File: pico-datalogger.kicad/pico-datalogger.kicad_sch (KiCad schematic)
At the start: 15 parts, among them J1 JST-PH2 VCC, J4 Alt-VCC, SW1 SW_Push_SLIM, U1 SN74HC74N, Y1 Crystal

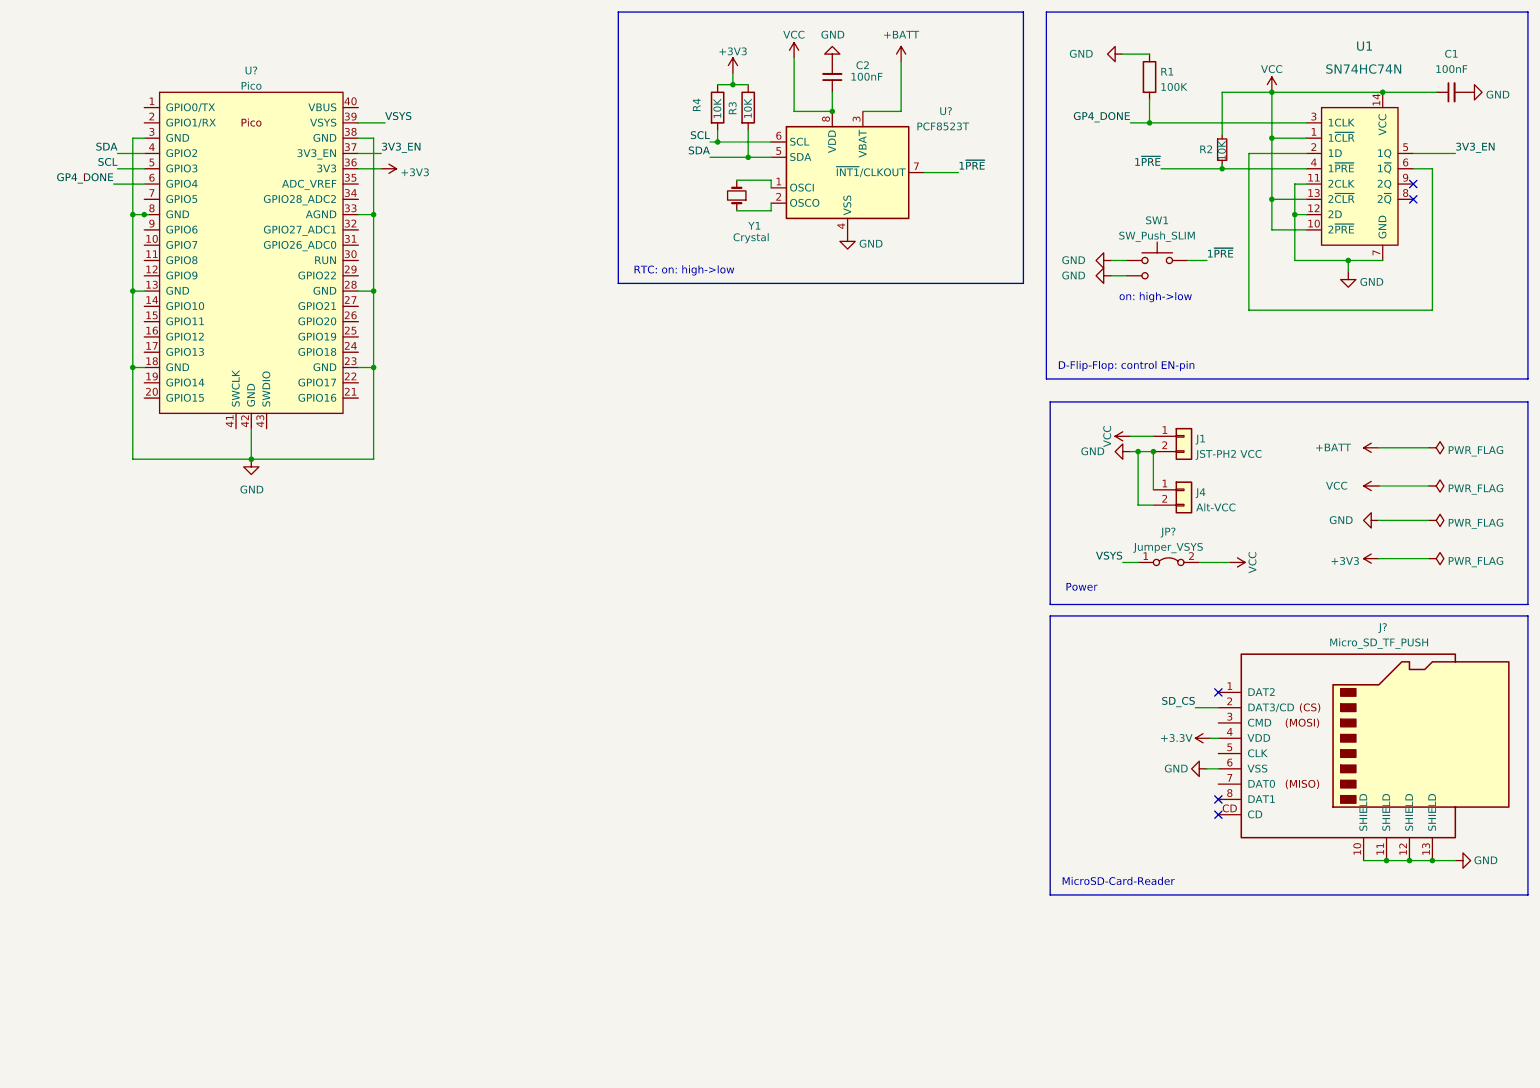
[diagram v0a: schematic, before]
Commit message: added battery and connectors
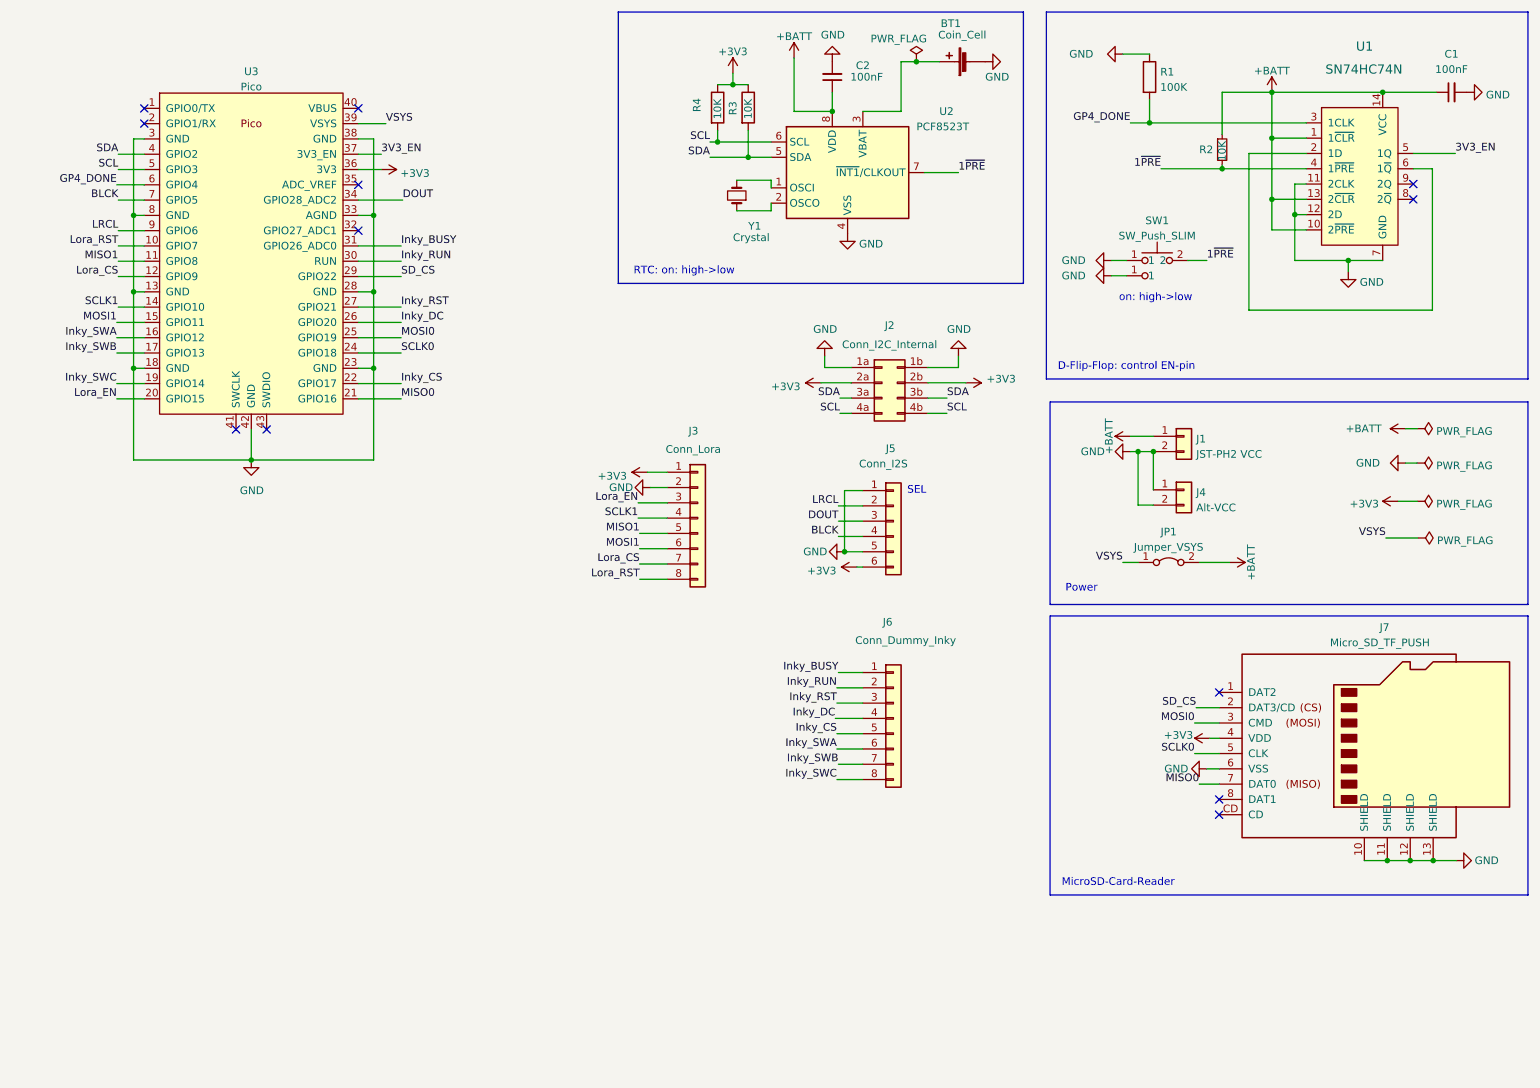
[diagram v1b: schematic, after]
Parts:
- added BT1: Coin_Cell, symbol Device:Battery_Cell
- added J2: Conn_I2C_Internal, symbol Connector_Generic:Conn_02x04_Row_Letter_Last
- added J3: Conn_Lora, symbol Connector_Generic:Conn_01x08
- added J5: Conn_I2S, symbol Connector_Generic:Conn_01x06
- added J6: Conn_Dummy_Inky, symbol Connector_Generic:Conn_01x08
- gave numbers to parts that had none: 4
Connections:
- net +3.3V is gone; now on net +3V3: J7.4 (VDD)
- net VCC is gone; now on net +BATT: C1.1, C2.1, J1.1 (Pin_1), JP1.2 (B), R2.1, U1.1 (1~{CLR}), U1.10 (2~{PRE}), U1.13 (2~{CLR}), U1.14 (VCC), U2.8 (VDD)
- net +3V3: now also J2.2a (Pin_2a), J2.2b (Pin_2b), J3.1 (Pin_1), J5.6 (Pin_6)
- net +BATT: no longer U2.3 (VBAT)
- net GND: now also BT1.2 (-), J2.1a (Pin_1a), J2.1b (Pin_1b), J3.2 (Pin_2), J5.1 (Pin_1), J5.5 (Pin_5); no longer SW1.3 (1)
- net SCL: now also J2.4a (Pin_4a), J2.4b (Pin_4b)
- net SDA: now also J2.3a (Pin_3a), J2.3b (Pin_3b)
- net SD_CS: now also U3.29 (GPIO22)
- net MOSI0: now reaches J7.3 (CMD)
- net MOSI0: now also U3.25 (GPIO19)
- net SCLK0: now reaches J7.5 (CLK)
- net SCLK0: now also U3.24 (GPIO18)
- net MISO0: now reaches J7.7 (DAT0)
- net MISO0: now also U3.21 (GPIO16)
- net Lora_RST: now reaches U3.10 (GPIO7)
- net Lora_RST: now also J3.8 (Pin_8)
- net MISO1: now reaches U3.11 (GPIO8)
- net MISO1: now also J3.5 (Pin_5)
- net Lora_CS: now reaches U3.12 (GPIO9)
- net Lora_CS: now also J3.7 (Pin_7)
- net SCLK1: now reaches U3.14 (GPIO10)
- net SCLK1: now also J3.4 (Pin_4)
- net MOSI1: now reaches U3.15 (GPIO11)
- net MOSI1: now also J3.6 (Pin_6)
- net Inky_SWA: now reaches U3.16 (GPIO12)
- net Inky_SWA: now also J6.6 (Pin_6)
- net Inky_SWB: now reaches U3.17 (GPIO13)
- net Inky_SWB: now also J6.7 (Pin_7)
- net Inky_SWC: now reaches U3.19 (GPIO14)
- net Inky_SWC: now also J6.8 (Pin_8)
- net Lora_EN: now reaches U3.20 (GPIO15)
- net Lora_EN: now also J3.3 (Pin_3)
- net Inky_CS: now reaches U3.22 (GPIO17)
- net Inky_CS: now also J6.5 (Pin_5)
- net Inky_DC: now reaches U3.26 (GPIO20)
- net Inky_DC: now also J6.4 (Pin_4)
- net Inky_RST: now reaches U3.27 (GPIO21)
- net Inky_RST: now also J6.3 (Pin_3)
- net Inky_RUN: now reaches U3.30 (RUN)
- net Inky_RUN: now also J6.2 (Pin_2)
- net Inky_BUSY: now reaches U3.31 (GPIO26_ADC0)
- net Inky_BUSY: now also J6.1 (Pin_1)
- net DOUT: now reaches U3.34 (GPIO28_ADC2)
- net DOUT: now also J5.3 (Pin_3)
- net BLCK: now reaches U3.7 (GPIO5)
- net BLCK: now also J5.4 (Pin_4)
- net LRCL: now reaches U3.9 (GPIO6)
- net LRCL: now also J5.2 (Pin_2)
- new net: BT1.1 (+), U2.3 (VBAT)
- no-connect marks 5 -> 12
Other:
- note added: "SEL"

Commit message: Rev. 0.8: components with footprints
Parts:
- BT1: footprint (none) -> user:CR2032_Holder; LCSC (none) -> C964777
- J2: footprint (none) -> Connector_PinHeader_2.54mm:PinHeader_2x04_P2.54mm_Vertical; now left out of the parts list
- J3: value Conn_Lora -> RFM9x_Lora_Breakout; footprint (none) -> user:RFM9x_Lora_Breakout; symbol Connector_Generic:Conn_01x08 -> user:RFM9x_Lora_Breakout
- J5: footprint (none) -> Connector_PinHeader_2.54mm:PinHeader_1x06_P2.54mm_Vertical; now left out of the parts list
- J6, U3: now left out of the parts list
- JP1: footprint (none) -> user:CR2032_Holder
- U2: LCSC C7440 -> C2651516
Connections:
- net Lora_CS: now also J3.8 (CS); no longer J3.7 (Pin_7)
- net Lora_RST: now also J3.9 (RST); no longer J3.8 (Pin_8)
- net MISO1: now also J3.6 (MISO); no longer J3.5 (Pin_5)
- net MOSI1: now also J3.7 (MOSI); no longer J3.6 (Pin_6)
- net SCLK1: now also J3.5 (SCK); no longer J3.4 (Pin_4)
- no-connect marks 12 -> 18
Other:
- note added: "Connectors (addons)"
- note added: "Connectors (internal)"
- note added: "Pico (2x20 Header)"
- moved on the sheet: J5, J6, U3

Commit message: Rev. 0.9: initial routing
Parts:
- J2: symbol Connector_Generic:Conn_02x04_Row_Letter_Last -> Connector_Generic:Conn_02x04_Odd_Even; now in the parts list
- JP1: footprint user:CR2032_Holder -> Connector_PinHeader_2.54mm:PinHeader_1x02_P2.54mm_Vertical
- U3: footprint RPi_Pico:RPi_Pico_SMD_TH -> user:RPi_Pico_TH_nodbg
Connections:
- net +3V3: now also J2.3 (Pin_3), J2.4 (Pin_4); no longer J2.2a (Pin_2a), J2.2b (Pin_2b)
- net +BATT: now also J4.1 (Pin_1)
- net GND: now also J2.1 (Pin_1), J2.2 (Pin_2); no longer J2.1a (Pin_1a), J2.1b (Pin_1b), J4.1 (Pin_1)
- net SCL: now also J2.7 (Pin_7), J2.8 (Pin_8); no longer J2.4a (Pin_4a), J2.4b (Pin_4b)
- net SDA: now also J2.5 (Pin_5), J2.6 (Pin_6); no longer J2.3a (Pin_3a), J2.3b (Pin_3b)

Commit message: Rev. 0.95: review for production
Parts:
- added H1, H2, H3, H4: MountingHole, MountingHole:MountingHole_2.5mm, symbol Mechanical:MountingHole
- added J10: Conn_Inky_SW, Connector_PinHeader_2.54mm:PinHeader_1x03_P2.54mm_Vertical, symbol Connector_Generic:Conn_01x03
- added J8: Conn_ADC, Connector_PinHeader_2.54mm:PinHeader_1x03_P2.54mm_Horizontal, symbol Connector_Generic:Conn_01x03
- added J9: Conn_UART, Connector_PinHeader_2.54mm:PinHeader_1x04_P2.54mm_Horizontal, symbol Connector_Generic:Conn_01x04
- J6: value Conn_Dummy_Inky -> Conn_Inky_SPI; footprint (none) -> Connector_PinHeader_2.54mm:PinHeader_1x08_P2.54mm_Vertical
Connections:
- net +3V3: now also J8.1 (Pin_1), J9.3 (Pin_3)
- net GND: now also J8.2 (Pin_2), J9.4 (Pin_4)
- net Inky_CS: now also J6.7 (Pin_7); no longer J6.5 (Pin_5)
- net Inky_SWA: now also J10.1 (Pin_1); no longer J6.6 (Pin_6)
- net Inky_SWB: now also J10.2 (Pin_2); no longer J6.7 (Pin_7)
- net Inky_SWC: now also J10.3 (Pin_3); no longer J6.8 (Pin_8)
- net MISO0: now also J6.8 (Pin_8)
- net MOSI0: now also J6.5 (Pin_5)
- net SCLK0: now also J6.6 (Pin_6)
- net TX: now reaches U3.1 (GPIO0/TX)
- net TX: now also J9.2 (Pin_2)
- net RX: now reaches U3.2 (GPIO1/RX)
- net RX: now also J9.1 (Pin_1)
- net GP27_ADC1: now reaches U3.32 (GPIO27_ADC1)
- net GP27_ADC1: now also J8.3 (Pin_3)
- no-connect marks 18 -> 15
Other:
- note added: "Connector Inky (optional)"
- note added: "Pico (2x20 Stacking-Header)"
- note removed: "Pico (2x20 Header)"
- moved on the sheet: J1, J4, J6

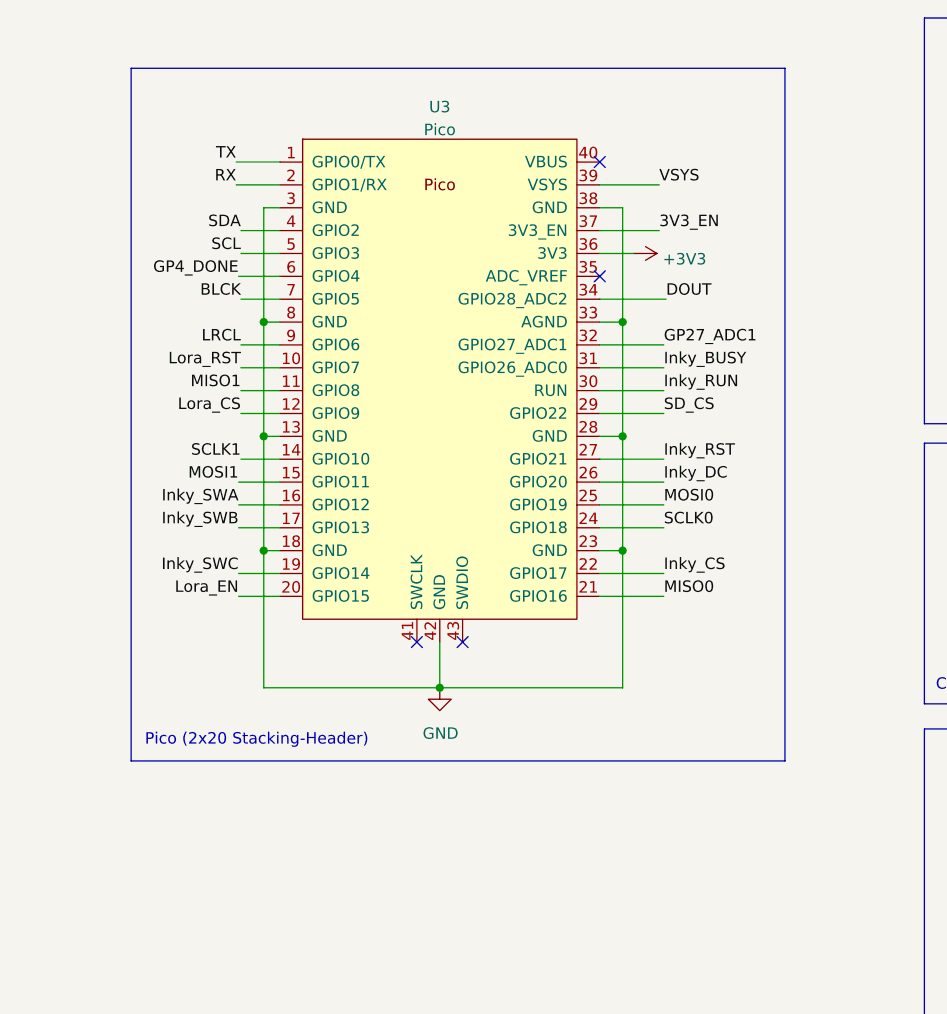
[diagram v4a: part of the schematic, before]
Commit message: Rev 0.96: added reset-button
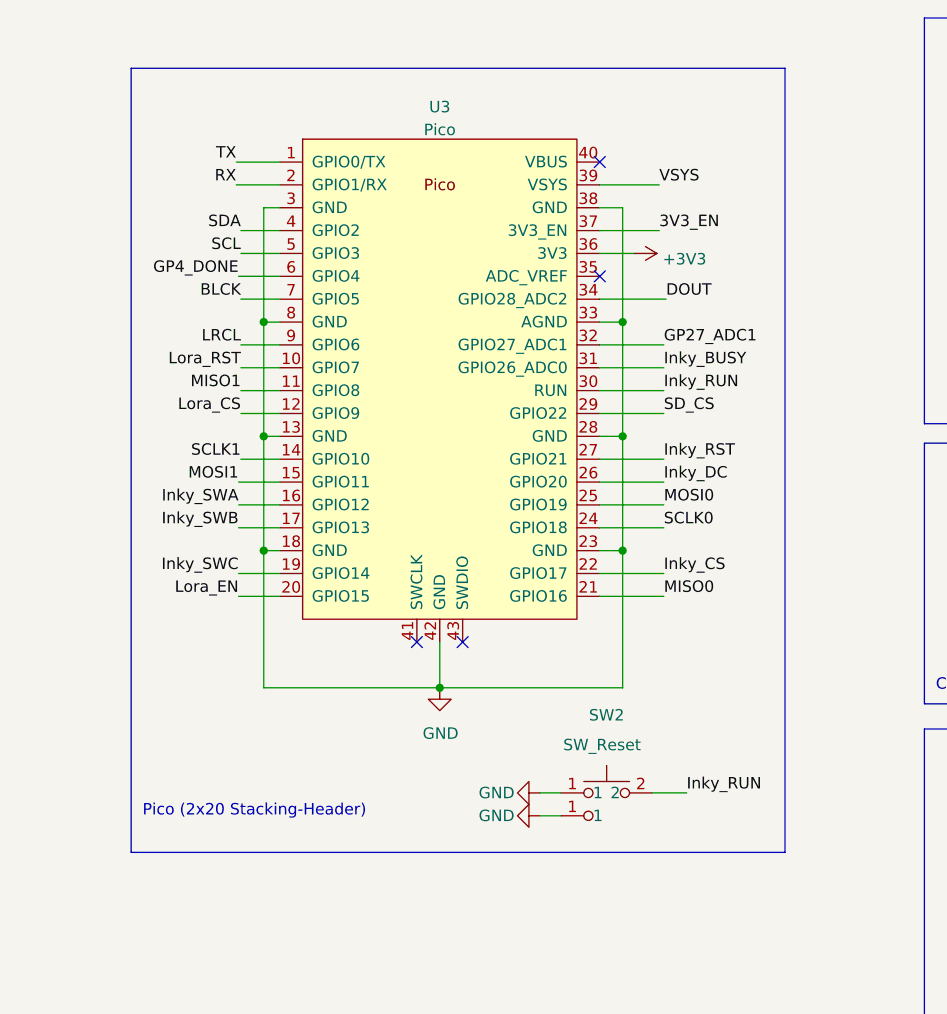
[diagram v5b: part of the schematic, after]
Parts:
- added SW2: SW_Reset, user:SW_PUSH_SLIM_1x4, symbol user:SW_Push_SLIM
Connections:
- net GND: now also SW2.1
- net Inky_RUN: now also SW2.2
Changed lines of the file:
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@@
   (title_block
     (title "pico-datalogger")
-    (date "2023-05-13")
-    (rev "0.95")
+    (date "2023-05-14")
+    (rev "0.96")
     (company "Bernhard Bablok")
     (comment 1 "https://github.com/bablokb/pcb-pico-datalogger")
@@
     (stroke (width 0) (type default) (color 0 0 0 0))
   )
+  (wire (pts (xy 85.598 106.426) (xy 87.884 106.426))
+    (stroke (width 0) (type default) (color 0 0 0 0))
+  )
   (wire (pts (xy 138.938 119.126) (xy 143.51 119.126))
     (stroke (width 0) (type default) (color 0 0 0 0))
@@
     (stroke (width 0) (type default) (color 0 0 0 0))
   )
-  (polyline (pts (xy 40.132 23.368) (xy 40.132 100.33))
+  (polyline (pts (xy 40.132 23.368) (xy 40.132 110.49))
     (stroke (width 0) (type default) (color 0 0 0 0))
   )
@@
     (stroke (width 0) (type default) (color 0 0 0 0))
   )
-  (polyline (pts (xy 112.776 23.368) (xy 112.776 100.33))
+  (polyline (pts (xy 112.776 23.368) (xy 112.776 110.49))
     (stroke (width 0) (type default) (color 0 0 0 0))
   )
@@
     (stroke (width 0) (type default) (color 0 0 0 0))
   )
+  (wire (pts (xy 101.854 103.886) (xy 98.044 103.886))
+    (stroke (width 0) (type default) (color 0 0 0 0))
+  )
   (wire (pts (xy 99.314 74.422) (xy 92.202 74.422))
     (stroke (width 0) (type default) (color 0 0 0 0))
@@
     (stroke (width 0) (type default) (color 0 0 0 0))
   )
-  (polyline (pts (xy 112.776 100.33) (xy 40.132 100.33))
+  (polyline (pts (xy 112.776 110.49) (xy 40.132 110.49))
     (stroke (width 0) (type default) (color 0 0 0 0))
   )
@@
     (stroke (width 0) (type default) (color 0 0 0 0))
   )
+  (wire (pts (xy 85.598 103.886) (xy 87.884 103.886))
+    (stroke (width 0) (type default) (color 0 0 0 0))
+  )
   (wire (pts (xy 153.67 50.8) (xy 147.955 50.8))
     (stroke (width 0) (type default) (color 0 0 0 0))
@@
     (effects (font (size 1.27 1.27)) (justify left bottom))
   )
-  (text "Pico (2x20 Stacking-Header)" (at 41.656 98.806 0)
+  (text "Pico (2x20 Stacking-Header)" (at 41.402 106.68 0)
     (effects (font (size 1.27 1.27)) (justify left bottom))
   )
@@
   (label "VSYS" (at 212.09 109.22 180)
     (effects (font (size 1.27 1.27)) (justify right bottom))
+  )
+  (label "Inky_RUN" (at 101.854 103.886 0)
+    (effects (font (size 1.27 1.27)) (justify left bottom))
   )
   (label "SCL" (at 52.324 43.942 180)
@@
     )
     (property "Datasheet" "" (id 3) (at 180.594 127.762 0)
+      (effects (font (size 1.27 1.27)) hide)
+    )
+    (pin "1")
+  )
+  (symbol (lib_id "power:GND") (at 85.598 103.886 270) (unit 1)
+    (in_bom yes) (on_board yes)
+    (property "Reference" "#PWR029" (id 0) (at 79.248 103.886 0)
+      (effects (font (size 1.27 1.27)) hide)
+    )
+    (property "Value" "GND" (id 1) (at 78.74 103.886 90)
+      (effects (font (size 1.27 1.27)) (justify left))
+    )
+    (property "Footprint" "" (id 2) (at 85.598 103.886 0)
+      (effects (font (size 1.27 1.27)) hide)
+    )
+    (property "Datasheet" "" (id 3) (at 85.598 103.886 0)
       (effects (font (size 1.27 1.27)) hide)
     )
@@
     )
     (pin "1")
+  )
+  (symbol (lib_id "user:SW_Push_SLIM") (at 92.964 103.886 0) (unit 1)
+    (in_bom yes) (on_board yes)
+    (property "Reference" "SW2" (id 0) (at 92.964 95.25 0))
+    (property "Value" "SW_Reset" (id 1) (at 92.456 98.552 0))
+    (property "Footprint" "user:SW_PUSH_SLIM_1x4" (id 2) (at 92.964 111.506 0)
+      (effects (font (size 1.27 1.27)) hide)
+    )
+    (property "Datasheet" "" (id 3) (at 92.964 98.806 0)
+      (effects (font (size 1.27 1.27)) hide)
+    )
+    (pin "1")
+    (pin "1")
+    (pin "2")
   )
   (symbol (lib_id "power:GND") (at 189.23 26.035 90) (unit 1)
@@
     )
     (property "Datasheet" "" (id 3) (at 142.24 83.82 0)
+      (effects (font (size 1.27 1.27)) hide)
+    )
+    (pin "1")
+  )
+  (symbol (lib_id "power:GND") (at 85.598 106.426 270) (unit 1)
+    (in_bom yes) (on_board yes)
+    (property "Reference" "#PWR030" (id 0) (at 79.248 106.426 0)
+      (effects (font (size 1.27 1.27)) hide)
+    )
+    (property "Value" "GND" (id 1) (at 78.74 106.426 90)
+      (effects (font (size 1.27 1.27)) (justify left))
+    )
+    (property "Footprint" "" (id 2) (at 85.598 106.426 0)
+      (effects (font (size 1.27 1.27)) hide)
+    )
+    (property "Datasheet" "" (id 3) (at 85.598 106.426 0)
       (effects (font (size 1.27 1.27)) hide)
     )
@@
       (reference "#PWR028") (unit 1) (value "GND") (footprint "")
     )
+    (path "/3a69fcdf-0d3f-408d-9e78-fe946a77373b"
+      (reference "#PWR029") (unit 1) (value "GND") (footprint "")
+    )
+    (path "/80196391-62f7-40aa-8fc9-a3a90aca579b"
+      (reference "#PWR030") (unit 1) (value "GND") (footprint "")
+    )
     (path "/ac7dda72-ef93-47f8-ba8e-cc7eb10e88fc"
       (reference "#PWR0101") (unit 1) (value "+3V3") (footprint "")
@@
       (reference "SW1") (unit 1) (value "SW_Push_SLIM") (footprint "user:SW_PUSH_SLIM_1x4")
     )
+    (path "/49d15796-03e7-43de-9903-aa7b35d5590c"
+      (reference "SW2") (unit 1) (value "SW_Reset") (footprint "user:SW_PUSH_SLIM_1x4")
+    )
     (path "/aeee191c-38fd-4ab0-b212-9eafb9d35bdc"
